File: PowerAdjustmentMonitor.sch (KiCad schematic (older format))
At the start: 36 parts, among them U11 LM317, U6 LM337T, U8 LM337T, U9 LM317

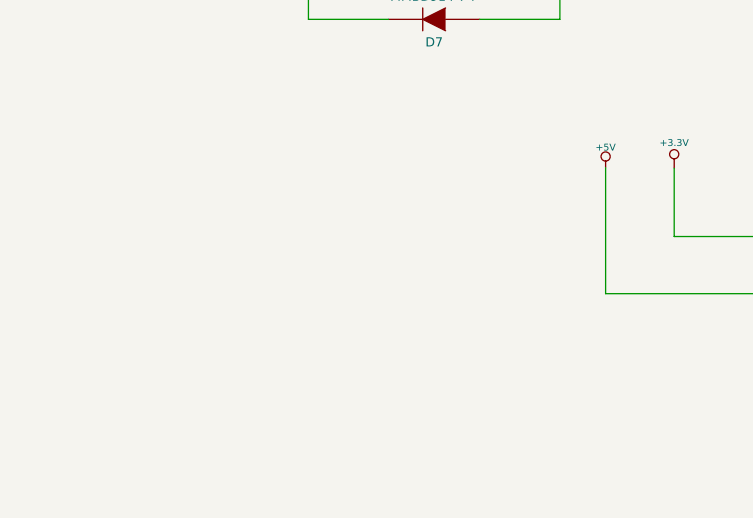
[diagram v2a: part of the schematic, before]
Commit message: Layout Work Session 16
Added ground connect to heatsink, fixed relay trace width, fixed silk
screen issues.
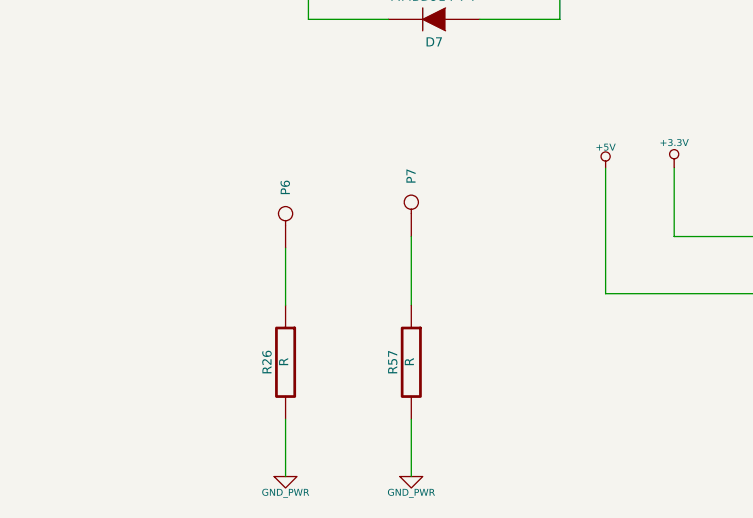
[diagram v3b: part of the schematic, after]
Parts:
- added P6, P7: CONN_1, symbol CONN_1
- added R26, R57: R, ~, symbol R
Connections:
- wire segments 103 -> 107
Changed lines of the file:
@@
-EESchema Schematic File Version 2  date 11/24/2013 8:21:44 PM
+EESchema Schematic File Version 2  date 12/1/2013 9:10:28 PM
 LIBS:power
 LIBS:device
@@
 Sheet 5 9
 Title ""
-Date "24 nov 2013"
+Date "2 dec 2013"
 Rev ""
 Comp ""
@@
 $EndDescr
 $Comp
-L +3.3V #PWR021
+L +3.3V #PWR31
 U 1 1 523E00C5
 P 3900 5700
-F 0 "#PWR021" H 3900 5660 30  0001 C CNN
+F 0 "#PWR31" H 3900 5660 30  0001 C CNN
 F 1 "+3.3V" H 3900 5810 30  0000 C CNN
 F 2 "" H 3900 5700 60  0000 C CNN
@@
 $EndComp
 $Comp
-L +5V #PWR022
+L +5V #PWR30
 U 1 1 523E00CB
 P 3600 5700
-F 0 "#PWR022" H 3600 5790 20  0001 C CNN
+F 0 "#PWR30" H 3600 5790 20  0001 C CNN
 F 1 "+5V" H 3600 5790 30  0000 C CNN
 F 2 "" H 3600 5700 60  0000 C CNN
@@
 $EndComp
 $Comp
-L -12V #PWR023
+L -12V #PWR25
 U 1 1 523E0153
 P 1100 4400
-F 0 "#PWR023" H 1100 4530 20  0001 C CNN
+F 0 "#PWR25" H 1100 4530 20  0001 C CNN
 F 1 "-12V" H 1100 4500 30  0000 C CNN
 F 2 "" H 1100 4400 60  0000 C CNN
@@
 $EndComp
 $Comp
-L +12V #PWR024
+L +12V #PWR35
 U 1 1 523E015D
 P 6400 1700
-F 0 "#PWR024" H 6400 1650 20  0001 C CNN
+F 0 "#PWR35" H 6400 1650 20  0001 C CNN
 F 1 "+12V" H 6400 1800 30  0000 C CNN
 F 2 "" H 6400 1700 60  0000 C CNN
@@
 $EndComp
 $Comp
-L FE_V+ #PWR025
+L FE_V+ #PWR32
 U 1 1 523E0975
 P 4950 1800
-F 0 "#PWR025" H 4950 1900 30  0001 C CNN
+F 0 "#PWR32" H 4950 1900 30  0001 C CNN
 F 1 "FE_V+" H 4950 1900 30  0000 C CNN
 F 2 "~" H 4950 1800 60  0000 C CNN
@@
 $EndComp
 $Comp
-L FE_V- #PWR30
+L FE_V- #PWR33
 U 1 1 523E099B
 P 4950 4450
-F 0 "#PWR30" H 4950 4650 40  0001 C CNN
+F 0 "#PWR33" H 4950 4650 40  0001 C CNN
 F 1 "FE_V-" H 4950 4600 40  0000 C CNN
 F 2 "~" H 4950 4450 60  0000 C CNN
@@
 Connection ~ 3750 3150
 $Comp
-L GND_PWR #PWR026
+L GND_PWR #PWR36
 U 1 1 527CFD60
 P 6550 3900
-F 0 "#PWR026" H 6550 3900 30  0001 C CNN
+F 0 "#PWR36" H 6550 3900 30  0001 C CNN
 F 1 "GND_PWR" H 6550 3830 30  0000 C CNN
 F 2 "~" H 6550 3900 60  0000 C CNN
@@
 $EndComp
 $Comp
-L -12V #PWR027
+L -12V #PWR34
 U 1 1 527CFD7C
 P 5950 5250
-F 0 "#PWR027" H 5950 5380 20  0001 C CNN
+F 0 "#PWR34" H 5950 5380 20  0001 C CNN
 F 1 "-12V" H 5950 5350 30  0000 C CNN
 F 2 "" H 5950 5250 60  0000 C CNN
@@
 	1550 4050 1550 4700
 $Comp
-L +12V #PWR028
+L +12V #PWR27
 U 1 1 527CFEC0
 P 1500 1700
-F 0 "#PWR028" H 1500 1650 20  0001 C CNN
+F 0 "#PWR27" H 1500 1650 20  0001 C CNN
 F 1 "+12V" H 1500 1800 30  0000 C CNN
 F 2 "" H 1500 1700 60  0000 C CNN
@@
 Connection ~ 6800 3800
 $Comp
-L AGND #PWR029
+L AGND #PWR26
 U 1 1 527EFACA
 P 1250 3350
-F 0 "#PWR029" H 1250 3350 40  0001 C CNN
+F 0 "#PWR26" H 1250 3350 40  0001 C CNN
 F 1 "AGND" H 1250 3280 50  0000 C CNN
 F 2 "~" H 1250 3350 60  0000 C CNN
@@
 	1    0    0    -1
 $EndComp
+$Comp
+L R R26
+U 1 1 529BFA7C
+P 2200 6550
+F 0 "R26" V 2280 6550 40  0000 C CNN
+F 1 "R" V 2207 6551 40  0000 C CNN
+F 2 "~" V 2130 6550 30  0000 C CNN
+F 3 "~" H 2200 6550 30  0000 C CNN
+	1    2200 6550
+	-1   0    0    -1
+$EndComp
+$Comp
+L R R57
+U 1 1 529BFA82
+P 2750 6550
+F 0 "R57" V 2830 6550 40  0000 C CNN
+F 1 "R" V 2757 6551 40  0000 C CNN
+F 2 "~" V 2680 6550 30  0000 C CNN
+F 3 "~" H 2750 6550 30  0000 C CNN
+	1    2750 6550
+	-1   0    0    -1
+$EndComp
+$Comp
+L GND_PWR #PWR28
+U 1 1 529BFA88
+P 2200 7050
+F 0 "#PWR28" H 2200 7050 30  0001 C CNN
+F 1 "GND_PWR" H 2200 6980 30  0000 C CNN
+F 2 "~" H 2200 7050 60  0000 C CNN
+F 3 "~" H 2200 7050 60  0000 C CNN
+	1    2200 7050
+	1    0    0    -1
+$EndComp
+$Comp
+L GND_PWR #PWR29
+U 1 1 529BFA8E
+P 2750 7050
+F 0 "#PWR29" H 2750 7050 30  0001 C CNN
+F 1 "GND_PWR" H 2750 6980 30  0000 C CNN
+F 2 "~" H 2750 7050 60  0000 C CNN
+F 3 "~" H 2750 7050 60  0000 C CNN
+	1    2750 7050
+	1    0    0    -1
+$EndComp
+Wire Wire Line
+	2750 7050 2750 6800
+Wire Wire Line
+	2200 7050 2200 6800
+$Comp
+L CONN_1 P7
+U 1 1 529BFBD5
+P 2750 5850
+F 0 "P7" H 2830 5850 40  0000 L CNN
+F 1 "CONN_1" H 2750 5905 30  0001 C CNN
+F 2 "" H 2750 5850 60  0000 C CNN
+F 3 "" H 2750 5850 60  0000 C CNN
+	1    2750 5850
+	0    -1   -1   0
+$EndComp
+$Comp
+L CONN_1 P6
+U 1 1 529BFBEC
+P 2200 5900
+F 0 "P6" H 2280 5900 40  0000 L CNN
+F 1 "CONN_1" H 2200 5955 30  0001 C CNN
+F 2 "" H 2200 5900 60  0000 C CNN
+F 3 "" H 2200 5900 60  0000 C CNN
+	1    2200 5900
+	0    -1   -1   0
+$EndComp
+Wire Wire Line
+	2200 6050 2200 6300
+Wire Wire Line
+	2750 6000 2750 6300
 $EndSCHEMATC

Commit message: Layout Work Session 17 Output
Fixing the power modify section pinout.
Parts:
- removed U11, U9: LM317, ~, symbol LM317
- added U11, U9: LM317T, TO220_BB, symbol LM317T
- U6, U8: footprint TO-220 -> TO220_BB
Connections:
- wire segments 107 -> 105
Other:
- moved on the sheet: D12, D3
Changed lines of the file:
@@
-EESchema Schematic File Version 2  date 12/1/2013 9:10:28 PM
+EESchema Schematic File Version 2  date 12/3/2013 1:00:45 AM
 LIBS:power
 LIBS:device
@@
 Sheet 5 9
 Title ""
-Date "2 dec 2013"
+Date "3 dec 2013"
 Rev ""
 Comp ""
@@
 F 3 "~" H 4950 4450 60  0000 C CNN
 	1    4950 4450
-	1    0    0    -1
-$EndComp
-$Comp
-L LM317 U11
-U 1 1 523E0B74
-P 7550 2000
-F 0 "U11" H 7550 2300 60  0000 C CNN
-F 1 "LM317" H 7600 1750 60  0000 L CNN
-F 2 "~" H 7550 2000 60  0000 C CNN
-F 3 "~" H 7550 2000 60  0000 C CNN
-	1    7550 2000
 	1    0    0    -1
 $EndComp
@@
 $EndComp
 $Comp
-L LM317 U9
-U 1 1 525F3FCD
-P 3150 2100
-F 0 "U9" H 3150 2400 60  0000 C CNN
-F 1 "LM317" H 3200 1850 60  0000 L CNN
-F 2 "~" H 3150 2100 60  0000 C CNN
-F 3 "~" H 3150 2100 60  0000 C CNN
-	1    3150 2100
-	1    0    0    -1
-$EndComp
-$Comp
 L R R55
 U 1 1 525F3FD3
@@
 F 0 "U8" H 2650 4450 40  0000 C CNN
 F 1 "LM337T" H 2850 4450 40  0000 L CNN
-F 2 "TO-220" H 2850 4550 30  0000 C CIN
+F 2 "TO220_BB" H 2850 4550 30  0000 C CIN
 F 3 "~" H 2850 4650 60  0000 C CNN
 	1    2850 4650
@@
 F 0 "U6" H 7000 5200 40  0000 C CNN
 F 1 "LM337T" H 7200 5200 40  0000 L CNN
-F 2 "TO-220" H 7200 5300 30  0000 C CIN
+F 2 "TO220_BB" H 7200 5300 30  0000 C CIN
 F 3 "~" H 7200 5400 60  0000 C CNN
 	1    7200 5400
@@
 	8150 3800 8150 3000
 Wire Wire Line
-	7550 2350 7550 2450
+	7550 2150 7550 2450
 Wire Wire Line
 	7550 2450 8500 2450
@@
 	1500 1950 2750 1950
 Wire Wire Line
-	3150 2450 3150 2550
+	3150 2250 3150 2550
 Wire Wire Line
 	4950 1950 4950 1800
@@
 	4700 3150 4700 3700
 Connection ~ 4700 3150
-Connection ~ 4550 4700
 Wire Wire Line
 	9400 4650 9400 5450
@@
 Connection ~ 3900 1950
 Wire Wire Line
-	2850 4000 3650 4000
+	2850 4000 4150 4000
 $Comp
 L DIODE D12
 U 1 1 52660B34
-P 4150 3550
-F 0 "D12" H 4150 3650 40  0000 C CNN
-F 1 "MMBD914-7-F" H 4150 3450 40  0000 C CNN
-F 2 "~" H 4150 3550 60  0000 C CNN
-F 3 "~" H 4150 3550 60  0000 C CNN
-	1    4150 3550
+P 4150 4350
+F 0 "D12" H 4150 4450 40  0000 C CNN
+F 1 "MMBD914-7-F" H 4150 4250 40  0000 C CNN
+F 2 "~" H 4150 4350 60  0000 C CNN
+F 3 "~" H 4150 4350 60  0000 C CNN
+	1    4150 4350
 	0    -1   -1   0
 $EndComp
-Wire Wire Line
-	4150 3350 4150 3150
-Wire Wire Line
-	4150 3150 4700 3150
-Connection ~ 4200 3150
-Wire Wire Line
-	4150 3750 4150 3950
-Wire Wire Line
-	4150 3950 3650 3950
-Connection ~ 3650 3950
 $Comp
 L DIODE D7
@@
 F 3 "~" H 2850 5050 60  0000 C CNN
 	1    2850 5050
-	-1   0    0    1
+	1    0    0    -1
 $EndComp
 Wire Wire Line
@@
 L DIODE D3
 U 1 1 52660D76
-P 7150 5700
-F 0 "D3" H 7150 5800 40  0000 C CNN
-F 1 "MMBD914-7-F" H 7150 5600 40  0000 C CNN
-F 2 "~" H 7150 5700 60  0000 C CNN
-F 3 "~" H 7150 5700 60  0000 C CNN
-	1    7150 5700
-	-1   0    0    1
-$EndComp
-Wire Wire Line
-	7350 5700 7750 5700
-Wire Wire Line
-	7750 5700 7750 5450
+P 7150 5950
+F 0 "D3" H 7150 6050 40  0000 C CNN
+F 1 "MMBD914-7-F" H 7150 5850 40  0000 C CNN
+F 2 "~" H 7150 5950 60  0000 C CNN
+F 3 "~" H 7150 5950 60  0000 C CNN
+	1    7150 5950
+	1    0    0    -1
+$EndComp
+Wire Wire Line
+	7350 5950 7750 5950
+Wire Wire Line
+	7750 5950 7750 5450
 Connection ~ 7750 5450
 Wire Wire Line
-	6950 5700 6700 5700
-Wire Wire Line
-	6700 5700 6700 5450
+	6950 5950 6700 5950
+Wire Wire Line
+	6700 5950 6700 5450
 Connection ~ 6700 5450
 $Comp
@@
 Wire Wire Line
 	6400 1850 6400 1700
-Wire Wire Line
-	1250 3150 4200 3150
 Connection ~ 8000 3800
 Wire Wire Line
@@
 Wire Wire Line
 	2750 6000 2750 6300
+$Comp
+L LM317T U9
+U 1 1 529D78EC
+P 3150 2000
+F 0 "U9" H 2950 2200 40  0000 C CNN
+F 1 "LM317T" H 3150 2200 40  0000 L CNN
+F 2 "TO220_BB" H 3150 2100 30  0000 C CIN
+F 3 "~" H 3150 2000 60  0000 C CNN
+	1    3150 2000
+	1    0    0    -1
+$EndComp
+$Comp
+L LM317T U11
+U 1 1 529D799C
+P 7550 1900
+F 0 "U11" H 7350 2100 40  0000 C CNN
+F 1 "LM317T" H 7550 2100 40  0000 L CNN
+F 2 "TO220_BB" H 7550 2000 30  0000 C CIN
+F 3 "~" H 7550 1900 60  0000 C CNN
+	1    7550 1900
+	1    0    0    -1
+$EndComp
+Wire Wire Line
+	1250 3150 4700 3150
+Wire Wire Line
+	4150 4000 4150 4150
+Wire Wire Line
+	4150 4550 4150 4700
+Connection ~ 4150 4700
 $EndSCHEMATC

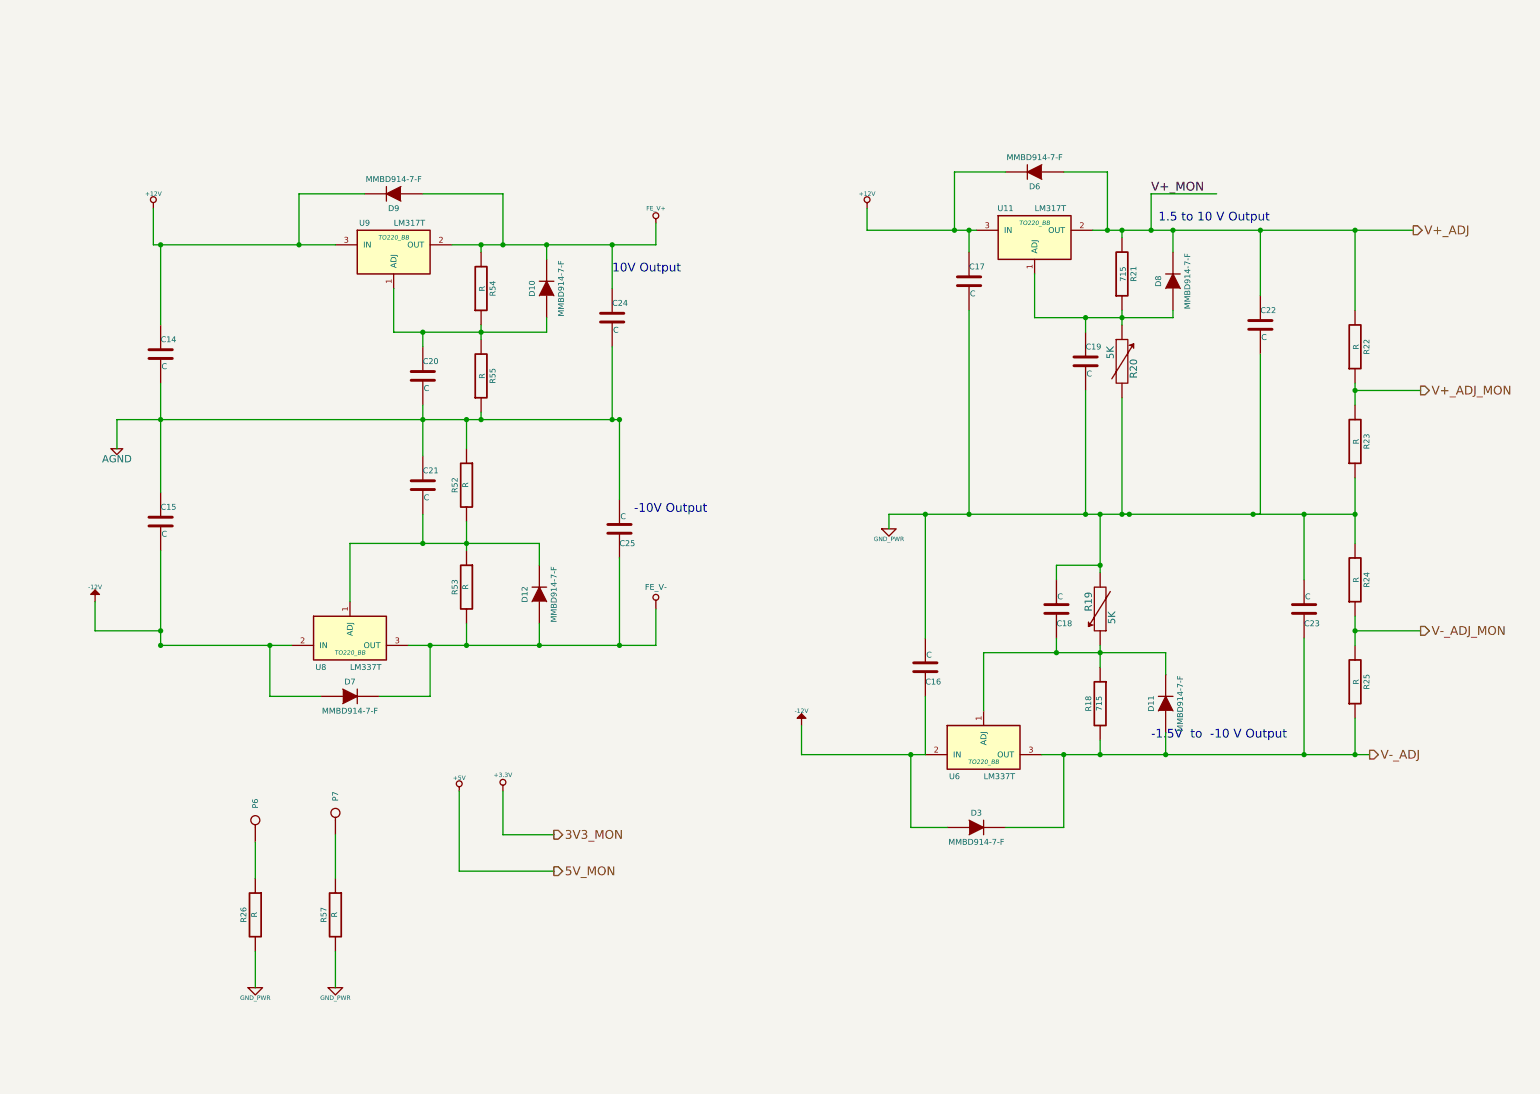
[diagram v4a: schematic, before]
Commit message: Layout Work Session 18 Output
Added test points, changed a bunch of silk screen, added another
mounting hole and added a placeholder for the final commit number of the
board being sent to fab.
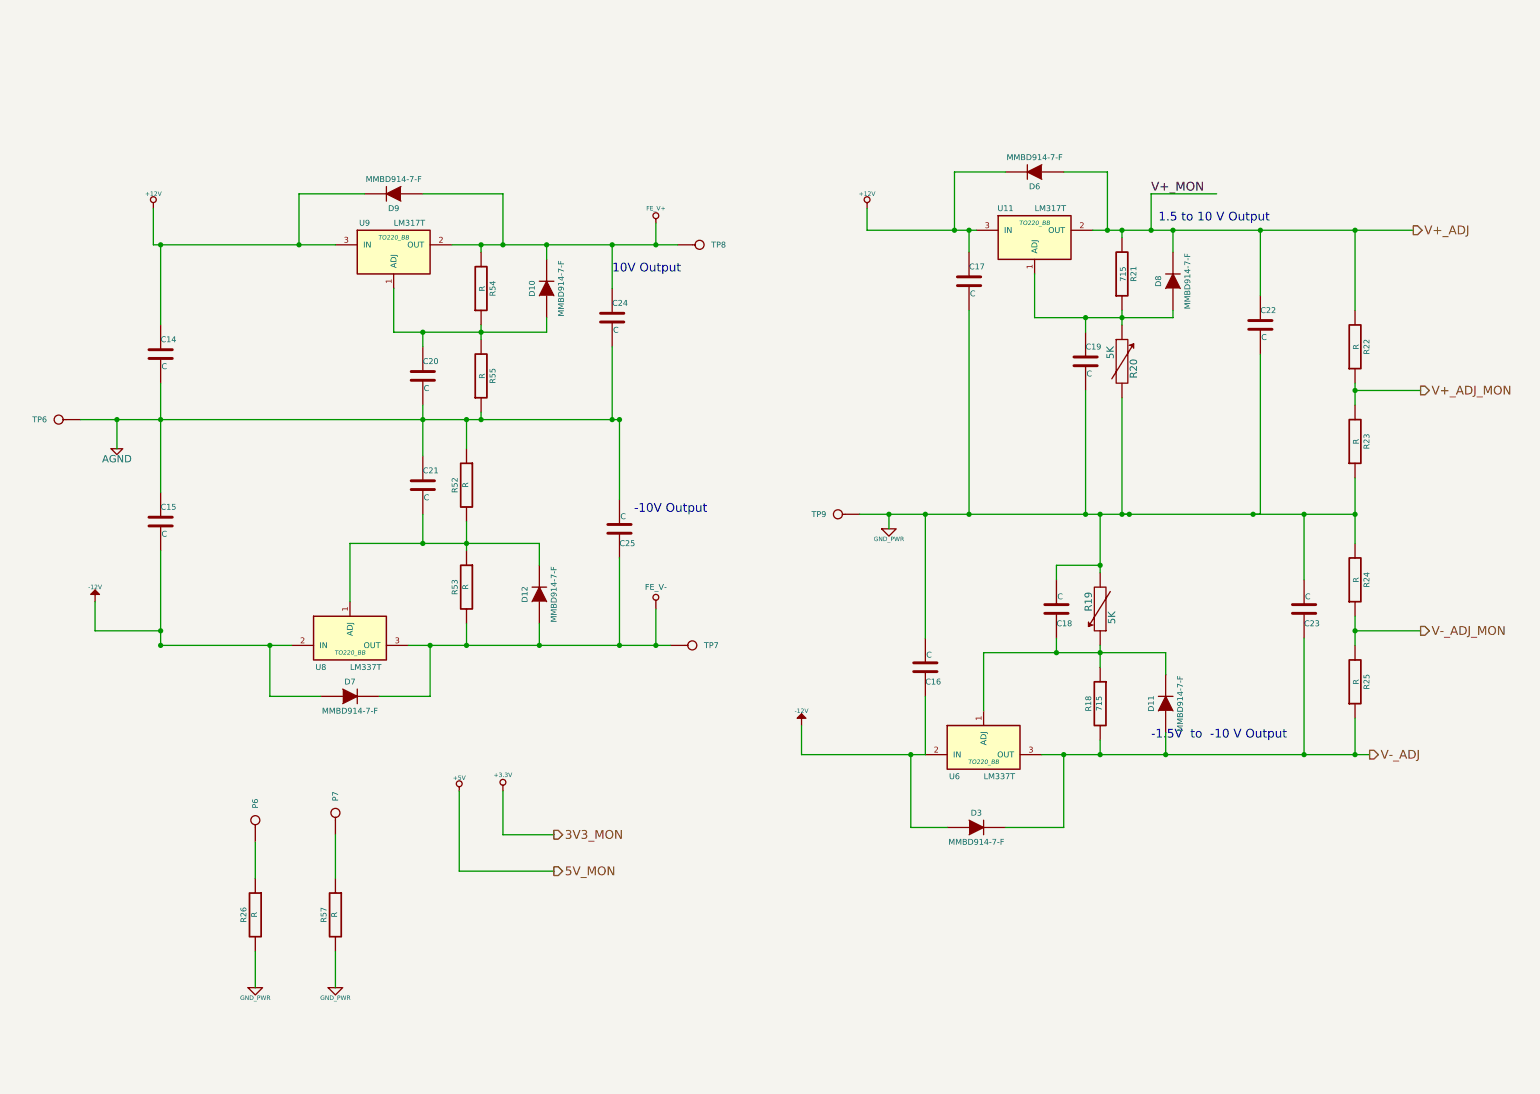
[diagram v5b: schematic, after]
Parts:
- added TP6: AGND, symbol CONN_1
- added TP7: FE_V-, symbol CONN_1
- added TP8: FE_V+, symbol CONN_1
- added TP9: GND_PWR, symbol CONN_1
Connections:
- net AGND: now also TP6.1
- net FE_V+: now also TP8.1
- net FE_V-: now also TP7.1
- net GND_PWR: now also TP9.1
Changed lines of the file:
@@
-EESchema Schematic File Version 2  date 12/3/2013 1:00:45 AM
+EESchema Schematic File Version 2  date 12/18/2013 11:27:15 PM
 LIBS:power
 LIBS:device
@@
 Sheet 5 9
 Title ""
-Date "3 dec 2013"
+Date "19 dec 2013"
 Rev ""
 Comp ""
@@
 	3750 1950 3750 2000
 Wire Wire Line
-	3550 1950 4950 1950
+	3550 1950 5100 1950
 Wire Wire Line
 	1500 1950 2750 1950
@@
 	9100 3800 9100 2700
 Wire Wire Line
-	6550 3800 9100 3800
+	6350 3800 9100 3800
 Connection ~ 8150 3800
 Wire Wire Line
@@
 	3150 2550 4200 2550
 Wire Wire Line
-	3250 4700 4950 4700
+	3250 4700 5050 4700
 Wire Wire Line
 	4700 4100 4700 4700
@@
 $EndComp
 Wire Wire Line
-	1250 3150 4700 3150
+	1000 3150 4700 3150
 Wire Wire Line
 	4150 4000 4150 4150
@@
 	4150 4550 4150 4700
 Connection ~ 4150 4700
+$Comp
+L CONN_1 TP9
+U 1 1 52B29910
+P 6200 3800
+F 0 "TP9" H 6280 3800 40  0000 L CNN
+F 1 "GND_PWR" H 6200 3855 30  0001 C CNN
+F 2 "" H 6200 3800 60  0000 C CNN
+F 3 "" H 6200 3800 60  0000 C CNN
+	1    6200 3800
+	-1   0    0    1
+$EndComp
+Connection ~ 6550 3800
+$Comp
+L CONN_1 TP8
+U 1 1 52B299D0
+P 5250 1950
+F 0 "TP8" H 5330 1950 40  0000 L CNN
+F 1 "FE_V+" H 5250 2005 30  0001 C CNN
+F 2 "" H 5250 1950 60  0000 C CNN
+F 3 "" H 5250 1950 60  0000 C CNN
+	1    5250 1950
+	1    0    0    -1
+$EndComp
+Connection ~ 4950 1950
+$Comp
+L CONN_1 TP7
+U 1 1 52B29A76
+P 5200 4700
+F 0 "TP7" H 5280 4700 40  0000 L CNN
+F 1 "FE_V-" H 5200 4755 30  0001 C CNN
+F 2 "" H 5200 4700 60  0000 C CNN
+F 3 "" H 5200 4700 60  0000 C CNN
+	1    5200 4700
+	1    0    0    -1
+$EndComp
+Connection ~ 4950 4700
+$Comp
+L CONN_1 TP6
+U 1 1 52B29E0B
+P 850 3150
+F 0 "TP6" H 930 3150 40  0000 L CNN
+F 1 "AGND" H 850 3205 30  0001 C CNN
+F 2 "" H 850 3150 60  0000 C CNN
+F 3 "" H 850 3150 60  0000 C CNN
+	1    850  3150
+	-1   0    0    1
+$EndComp
+Connection ~ 1250 3150
 $EndSCHEMATC
